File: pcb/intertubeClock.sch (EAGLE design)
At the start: 165 parts, among them Q1 BSA223SP, Q10 BSA223SP, Q11 BSA223SP, Q12 BSA223SP, Q13 BSA223SP, Q14 BSA223SP, Q15 BSA223SP, Q16 BSA223SP, Q2 BSA223SP, Q3 BSA223SP, Q4 BSA223SP, Q5 BSA223SP, Q6 BSA223SP, Q7 BSA223SP, Q8 BSA223SP, Q9 BSA223SP, U1 HV5122PG, U2 HV5122PG

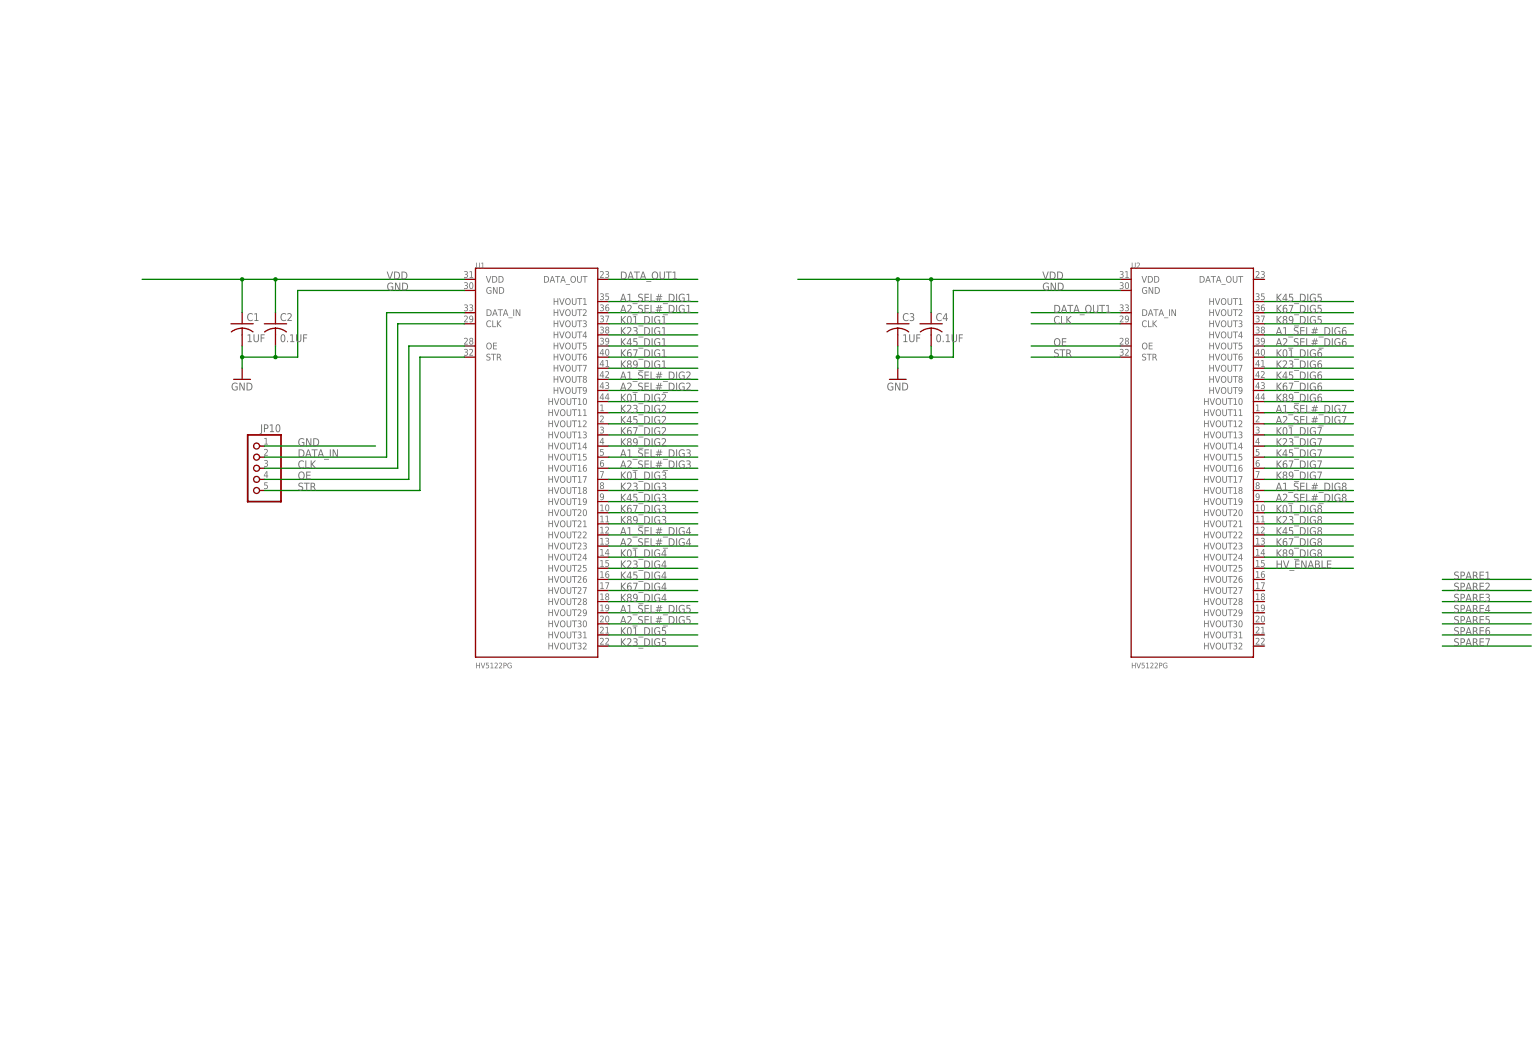
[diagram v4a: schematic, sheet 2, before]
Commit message: -ADDED LEVEL SHIFTER -BEGAN REPLACING DIODES
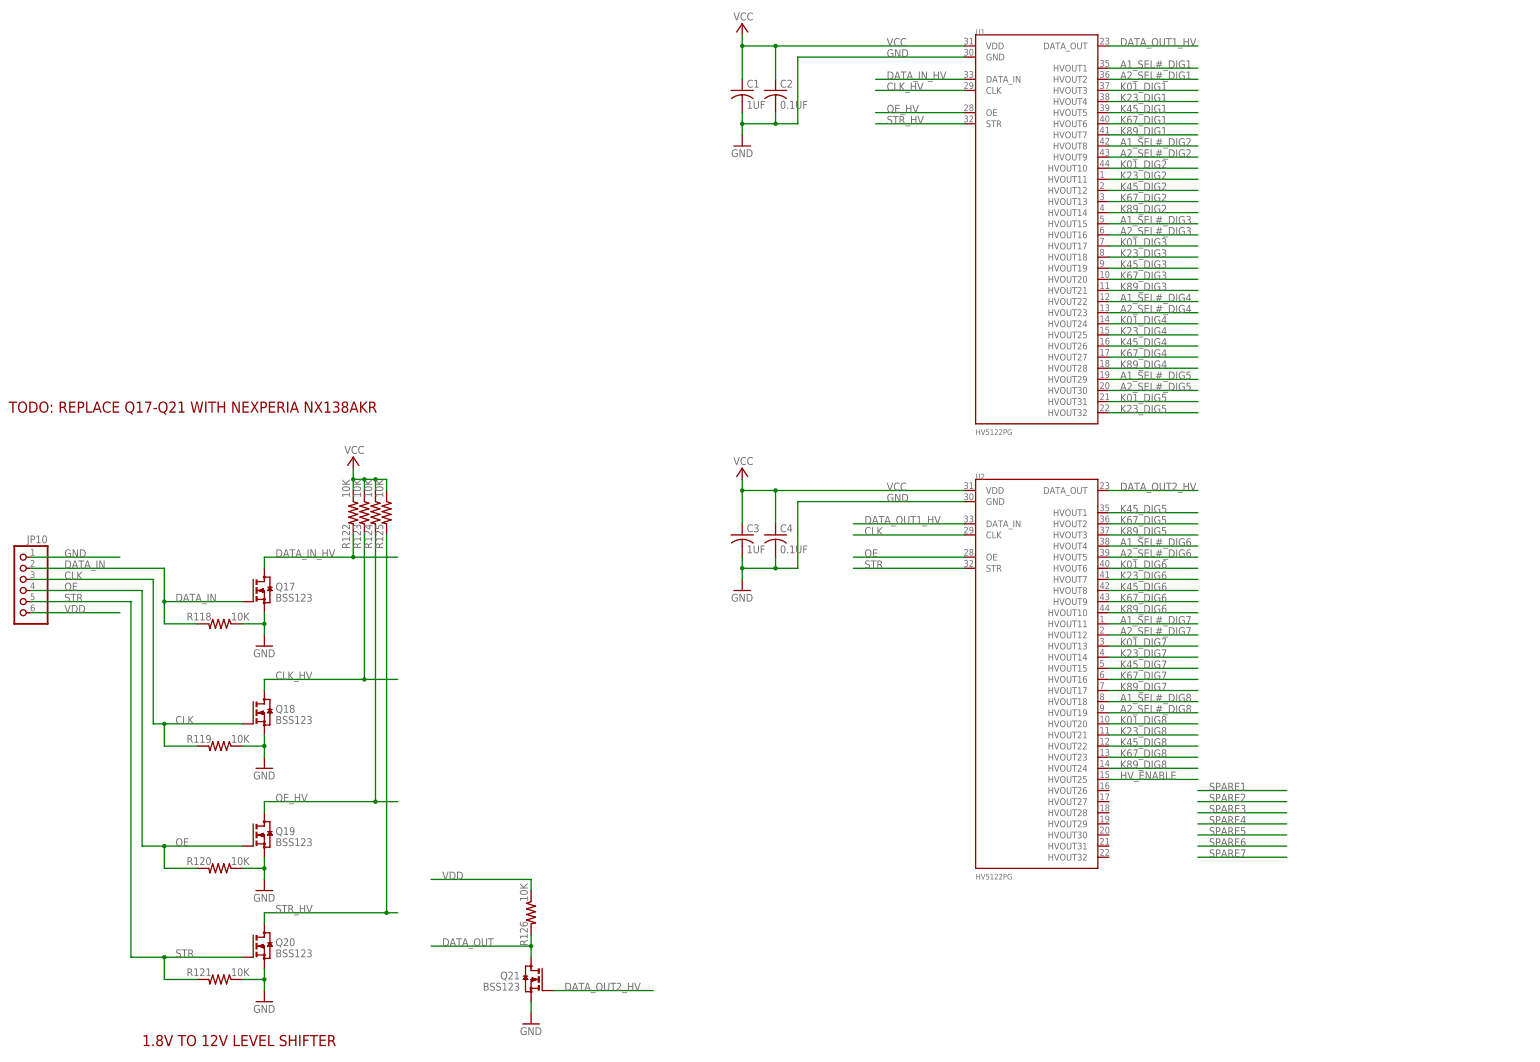
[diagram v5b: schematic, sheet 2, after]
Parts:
- removed D3, D4: GF1, diode:GF1
- added Q17, Q18, Q19, Q20, Q21: BSS123, transistor-small-signal:BSS123
- added R118, R119, R120, R121, R122, R123, R124, R125, R126: 10K, rcl:R-US_R0603
- D1, D2: value GF1 -> BAS40-06; device diode:GF1 -> diode:BAS40-06
- JP10: device pinhead:PINHD-1X5 -> pinhead:PINHD-1X6
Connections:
- net DATA_OUT1 renamed DATA_OUT1_HV
- new net CLK_HV: Q18.D, R123.2, U1.CLK
- new net DATA_IN_HV: Q17.D, R122.2, U1.DATA_IN
- new net DATA_OUT: Q21.D, R126.2
- new net DATA_OUT2_HV: Q21.G, U2.DATA_OUT
- new net OE_HV: Q19.D, R124.2, U1.OE
- new net STR_HV: Q20.D, R125.2, U1.STR
- new net VCC: C1.1, C2.1, C3.1, C4.1, R122.1, R123.1, R124.1, R125.1, U1.VDD, U2.VDD
- net CLK: now also Q18.G, R119.2; no longer U1.CLK
- net DATA_IN: now also Q17.G, R118.2; no longer U1.DATA_IN
- net GND: now also Q17.S, Q18.S, Q19.S, Q20.S, Q21.S, R118.1, R119.1, R120.1, R121.1
- net HV_VBA_OFF: now also D1.AA, D2.AA; no longer D1.A, D2.A, D3.A, D4.A
- net N$18: now also D1.K1; no longer D1.C
- net N$20: now also D1.K2; no longer D2.C
- net N$22: now also D2.K1; no longer D3.C
- net N$25: now also D2.K2; no longer D4.C
- net OE: now also Q19.G, R120.2; no longer U1.OE
- net STR: now also Q20.G, R121.2; no longer U1.STR
- net VDD: now also JP10.6, R126.1; no longer C1.1, C2.1, C3.1, C4.1, U1.VDD, U2.VDD
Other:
- note added: "1.8V TO 12V LEVEL SHIFTER"
- note added: "2019.05.05"
- note added: "300V DIODE: https://www.digikey.com/short/pz9qm0"
- note added: "ADDED LEVEL SHIFTER BEGAN REPLACING DIODES"
- note added: "TODO: REPLACE Q17-Q21 WITH NEXPERIA NX138AKR‎"
- moved on the sheet: C1, C2, C3, C4, U1, U2

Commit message: -PLACED NEW COMPONENTS.
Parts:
- removed D10, D11, D12, D13, D14, D15, D16, D9: GF1, diode:GF1
- added D3, D4: BAS40-06, diode:BAS40-06
- D5, D6, D7, D8: value GF1 -> BAS40-06; device diode:GF1 -> diode:BAS40-06
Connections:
- net HV_VBA_OFF: now also D3.AA, D4.AA, D5.AA, D6.AA, D7.AA, D8.AA; no longer D10.A, D11.A, D12.A, D13.A, D14.A, D15.A, D16.A, D5.A, D6.A, D7.A, D8.A, D9.A
- net N$26: now also D3.K1; no longer D5.C
- net N$27: now also D3.K2; no longer D6.C
- net N$28: now also D4.K1; no longer D7.C
- net N$29: now also D4.K2; no longer D8.C
- net N$31: now also D5.K1; no longer D9.C
- net N$32: now also D5.K2; no longer D10.C
- net N$33: now also D6.K1; no longer D11.C
- net N$34: now also D6.K2; no longer D12.C
- net N$36: now also D7.K1; no longer D13.C
- net N$37: now also D7.K2; no longer D14.C
- net N$38: now also D8.K1; no longer D15.C
- net N$39: now also D8.K2; no longer D16.C
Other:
- note added: "ADDED LEVEL SHIFTER BEGAN REPLACING DIODES PLACED NEW COMPONENTS"
- note removed: "ADDED LEVEL SHIFTER BEGAN REPLACING DIODES"
- moved on the sheet: Q13, Q14, Q15, Q16, Q5, Q6, Q7, Q8, R100, R101, R110, R111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

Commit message: -More layout work. -Added real parts library.
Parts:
- added JP11: Vba_off, pinhead:PINHD-1X2
- added JP12: Vba, pinhead:PINHD-1X2
- added JP13: Vs, pinhead:PINHD-1X2
- D1, D2, D3, D4, D5, D6, D7, D8: value BAS40-06 -> MMBD3004A; device diode:BAS40-06 -> intertubeClock:MMBD3004A
- JP2: value HV -> Vin; device pinhead:PINHD-1X4 -> pinhead:PINHD-1X2
- Q1, Q10, Q11, Q12, Q13, Q14, Q15, Q16, Q2, Q3, Q4, Q5, Q6, Q7, Q8, Q9: value BSA223SP -> TP5322K1-G; device transistor-fet:BSA223SP -> intertubeClock:TP5322K1-G
- Q17, Q18, Q19, Q20, Q21: value BSS123 -> NX138AK; device transistor-small-signal:BSS123 -> intertubeClock:NX138AK
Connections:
- new net N$40: D3.A
- net GND: now also JP11.1, JP12.1, JP13.1; no longer JP2.4
- net HV_IN: no longer JP2.3
- net HV_VBA: now also JP12.2
- net HV_VBA_OFF: now also D1.A, D2.A, D4.A, D5.A, D6.A, D7.A, D8.A, JP11.2; no longer D1.AA, D2.AA, D3.AA, D4.AA, D5.AA, D6.AA, D7.AA, D8.AA
- net HV_VS: now also JP13.2
- net N$22: now also D2.K2; no longer D2.K1
- net N$25: now also D2.K1; no longer D2.K2
- net N$26: now also D3.K2; no longer D3.K1
- net N$27: now also D3.K1; no longer D3.K2
- net N$28: now also D4.K2; no longer D4.K1
- net N$29: now also D4.K1; no longer D4.K2
- net N$31: now also D5.K2; no longer D5.K1
- net N$32: now also D5.K1; no longer D5.K2
- net N$33: now also D6.K2; no longer D6.K1
- net N$34: now also D6.K1; no longer D6.K2
- net N$36: now also D7.K2; no longer D7.K1
- net N$37: now also D7.K1; no longer D7.K2
- net N$38: now also D8.K2; no longer D8.K1
- net N$39: now also D8.K1; no longer D8.K2
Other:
- note added: "ADDED LEVEL SHIFTER BEGAN REPLACING DIODES PLACED NEW COMPONENTS REPLACED PLACEHOLDERS WITH REAL PARTS"
- note removed: "ADDED LEVEL SHIFTER BEGAN REPLACING DIODES PLACED NEW COMPONENTS"
- note removed: "TODO: REPLACE Q17-Q21 WITH NEXPERIA NX138AKR‎"
